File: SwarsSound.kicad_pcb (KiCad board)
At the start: 2 copper layers, 152 parts, among them P1 Main_Connector, P2 aud_con, P3 edge_con, Q1 2N3906f, Q2 2N3906f, Q3 2N3904, Q4 2N3904

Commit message: Moved a spot
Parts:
- moved P3 82.4 mm to (252.1, 123.9)

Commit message: Began board layout
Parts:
- added REF**: MountingHole2, Star_Wars_Vector_PCB:MountingHole2, F.Cu at (292.7, 39.4)
- added REF**: MountingHole2, Star_Wars_Vector_PCB:MountingHole2, F.Cu at (37.5, 47.0)
- added REF**: MountingHole, Star_Wars_Vector_PCB:MountingHole, F.Cu at (304.8, 24.1)
- added REF**: MountingHole, Star_Wars_Vector_PCB:MountingHole, F.Cu at (22.9, 24.1)
- added REF**: MountingHole, Star_Wars_Vector_PCB:MountingHole, F.Cu at (304.8, 240.0)
- added REF**: MountingHole, Star_Wars_Vector_PCB:MountingHole, F.Cu at (22.9, 240.0)
- moved P1 231.0 mm to (160.0, 225.8), turned to 180 degrees
- moved A-3 227.2 mm to (-49.0, 93.2)
- moved B-2 227.2 mm to (-38.9, 90.8)
- moved B-3 227.2 mm to (-151.5, 165.0)
- moved C-3 227.2 mm to (-81.0, 122.9)
- moved C-4 227.2 mm to (-91.1, 140.0)
- moved C/D-1 227.2 mm to (-128.0, 140.4)
- moved C1 227.2 mm to (-73.0, 150.5)
- moved C10 227.2 mm to (-67.2, 136.2)
- moved C11 227.2 mm to (-70.1, 136.2)
- moved C12 227.2 mm to (-89.0, 156.7)
- moved C16 227.2 mm to (-60.0, 127.8)
- moved C17 227.2 mm to (-39.6, 107.5)
- moved C18 227.2 mm to (-1.04, 69.4)
- moved C19 227.2 mm to (-22.2, 89.7)
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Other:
- board outline added: 292.1 x 227.3 mm

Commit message: Finished chip layout
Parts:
- removed H_2: LS04, Star_Wars_Vector_PCB:DIP14
- moved J/K-1 448.9 mm to (259.7, 73.7), turned to 180 degrees
- moved K-3 421.3 mm to (274.3, 128.3), turned to 180 degrees
- moved F/H-1 385.9 mm to (212.7, 71.1), turned to 180 degrees
- moved H-1 342.9 mm to (237.5, 73.7), turned to 180 degrees
- moved D-2 315.2 mm to (141.0, 119.4), turned to 90 degrees
- moved F-2 300.2 mm to (208.9, 114.3), turned to 180 degrees
- moved H-2 295.4 mm to (236.2, 114.3), turned to 180 degrees
- moved J-3 291.2 mm to (252.7, 138.4), turned to 180 degrees
- moved H-3 286.7 mm to (236.2, 140.3), turned to 180 degrees
- moved J-2 276.4 mm to (252.7, 113.0), turned to 180 degrees
- moved F-3 272.1 mm to (208.9, 138.4), turned to 180 degrees
- moved E-1 271.3 mm to (189.2, 87.6), turned to 180 degrees
- moved C/D-1 268.9 mm to (130.8, 67.3), turned to 180 degrees
- moved D-3 255.5 mm to (141.0, 143.5), turned to 90 degrees
- moved C32 249.2 mm to (106.7, 158.8), turned to 270 degrees
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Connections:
- A-3 pad 14: Net-(A-3-Pad14) -> +12V
- H-2 pad 10: (no net) -> ~SRES
- H-2 pad 11: (no net) -> Net-(F-5-Pad10)

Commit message: test
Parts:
- moved C27 41.9 mm to (43.2, 62.2)

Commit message: next push
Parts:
- added TP11: TP, Star_Wars_Vector_PCB:TEST_POINT, F.Cu at (207.0, 41.9)
- moved C2 310.5 mm to (259.1, 95.0), turned to 90 degrees
- moved R6 294.2 mm to (202.9, 34.0), turned to 90 degrees
- moved C5 287.5 mm to (184.9, 33.0), turned to 270 degrees
- moved R12 257.0 mm to (199.4, 110.5)
- moved C3 250.6 mm to (237.0, 95.0), turned to 90 degrees
- moved TP7 245.1 mm to (198.1, 41.9)
- moved C24 243.4 mm to (209.6, 102.9), turned to 90 degrees
- moved C4 243.1 mm to (211.6, 90.4), turned to 90 degrees
- moved R5 205.3 mm to (192.5, 44.5), turned to 180 degrees
- moved C27 39.4 mm to (3.81, 61.0)
- moved H-1 0.13 mm to (237.6, 73.7)
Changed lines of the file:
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@@
     (tracks 0)
     (zones 0)
-    (modules 157)
+    (modules 158)
     (nets 256)
   )
@@
     (add_net ɸE)
   )
+  (module Star_Wars_Vector_PCB:TEST_POINT (layer F.Cu)
+    (at 207.01 41.91)
+    (fp_text reference TP11 (at 0 0.635 90) (layer F.SilkS) hide
+      (effects (font (size 0.254 0.254) (thickness 0.0635)))
+    )
+    (fp_text value TP (at 0 -0.635 90) (layer F.Fab) hide
+      (effects (font (size 0.254 0.254) (thickness 0.0635)))
+    )
+    (pad 2 thru_hole circle (at 0 -2.54) (size 1.905 1.905) (drill 1.016) (layers *.Cu *.Mask)
+      (net 6 GND))
+    (pad 1 thru_hole circle (at 0 2.54) (size 1.905 1.905) (drill 1.016) (layers *.Cu *.Mask)
+      (net 6 GND))
+  )
   (module Star_Wars_Vector_PCB:MountingHole2 (layer F.Cu)
     (at 292.735 39.37)
@@
   )
   (module Star_Wars_Vector_PCB:TEST_POINT (layer F.Cu)
-    (at -20.3665 152.978499)
+    (at 198.12 41.91)
     (fp_text reference TP7 (at 0 0.635 90) (layer F.SilkS) hide
       (effects (font (size 0.254 0.254) (thickness 0.0635)))
@@
   )
   (module Star_Wars_Vector_PCB:GenericComp (layer F.Cu)
-    (at -55.6215 142.138499)
+    (at 199.39 110.49)
     (fp_text reference R12 (at 0 -9.525 90 unlocked) (layer F.SilkS)
       (effects (font (size 1 1) (thickness 0.15)))
@@
   )
   (module Star_Wars_Vector_PCB:GenericComp (layer F.Cu)
-    (at -67.2215 150.508499)
-    (fp_text reference R6 (at 0 -9.525 90 unlocked) (layer F.SilkS)
+    (at 202.946 34.036 90)
+    (fp_text reference R6 (at 0 -9.525 unlocked) (layer F.SilkS)
       (effects (font (size 1 1) (thickness 0.15)))
     )
-    (fp_text value 10K (at -1.27 -0.635 90) (layer F.Fab) hide
+    (fp_text value 10K (at -1.27 -0.635) (layer F.Fab) hide
       (effects (font (size 1 1) (thickness 0.15)))
     )
     (fp_line (start 0 -5.08) (end 0 3.81) (layer F.SilkS) (width 0.254))
-    (pad 2 thru_hole circle (at 0 -6.35) (size 1.905 1.905) (drill 1.016) (layers *.Cu *.Mask)
+    (pad 2 thru_hole circle (at 0 -6.35 90) (size 1.905 1.905) (drill 1.016) (layers *.Cu *.Mask)
       (net 129 "Net-(E-1-Pad12)"))
-    (pad 1 thru_hole circle (at 0 5.08) (size 1.905 1.905) (drill 1.016) (layers *.Cu *.Mask)
+    (pad 1 thru_hole circle (at 0 5.08 90) (size 1.905 1.905) (drill 1.016) (layers *.Cu *.Mask)
       (net 25 +5V))
   )
   (module Star_Wars_Vector_PCB:GenericComp (layer F.Cu)
-    (at -7.7215 89.535)
+    (at 192.532 44.45 180)
     (fp_text reference R5 (at 0 -9.525 90 unlocked) (layer F.SilkS)
       (effects (font (size 1 1) (thickness 0.15)))
@@
     )
     (fp_line (start 0 -5.08) (end 0 3.81) (layer F.SilkS) (width 0.254))
-    (pad 2 thru_hole circle (at 0 -6.35) (size 1.905 1.905) (drill 1.016) (layers *.Cu *.Mask)
+    (pad 2 thru_hole circle (at 0 -6.35 180) (size 1.905 1.905) (drill 1.016) (layers *.Cu *.Mask)
       (net 131 S~IRQ))
-    (pad 1 thru_hole circle (at 0 5.08) (size 1.905 1.905) (drill 1.016) (layers *.Cu *.Mask)
+    (pad 1 thru_hole circle (at 0 5.08 180) (size 1.905 1.905) (drill 1.016) (layers *.Cu *.Mask)
       (net 25 +5V))
   )
@@
   )
   (module Star_Wars_Main_PCB:DIP28 (layer F.Cu)
-    (at 237.49 73.66 180)
+    (at 237.617 73.66 180)
     (fp_text reference H-1 (at 0.635 -1.905 270 unlocked) (layer F.SilkS)
       (effects (font (size 1 1) (thickness 0.15)))
@@
   )
   (module Star_Wars_Vector_PCB:GenericComp (layer F.Cu)
-    (at 43.18 62.23)
+    (at 3.81 60.96)
     (fp_text reference C27 (at 0 -9.525 90 unlocked) (layer F.SilkS)
       (effects (font (size 1 1) (thickness 0.15)))
@@
   )
   (module Star_Wars_Vector_PCB:GenericComp (layer F.Cu)
-    (at -33.8015 107.508499)
-    (fp_text reference C24 (at 0 -9.525 90 unlocked) (layer F.SilkS)
+    (at 209.55 102.87 90)
+    (fp_text reference C24 (at 0 8.89 unlocked) (layer F.SilkS)
       (effects (font (size 1 1) (thickness 0.15)))
     )
-    (fp_text value 0.1 (at -1.27 -0.635 90) (layer F.Fab) hide
+    (fp_text value 0.1 (at -1.27 -0.635) (layer F.Fab) hide
       (effects (font (size 1 1) (thickness 0.15)))
     )
     (fp_line (start 0 -5.08) (end 0 3.81) (layer F.SilkS) (width 0.254))
-    (pad 2 thru_hole circle (at 0 -6.35) (size 1.905 1.905) (drill 1.016) (layers *.Cu *.Mask)
+    (pad 2 thru_hole circle (at 0 -6.35 90) (size 1.905 1.905) (drill 1.016) (layers *.Cu *.Mask)
       (net 6 GND))
-    (pad 1 thru_hole circle (at 0 5.08) (size 1.905 1.905) (drill 1.016) (layers *.Cu *.Mask)
+    (pad 1 thru_hole circle (at 0 5.08 90) (size 1.905 1.905) (drill 1.016) (layers *.Cu *.Mask)
       (net 12 -5V))
   )
@@
   )
   (module Star_Wars_Vector_PCB:GenericComp (layer F.Cu)
-    (at -75.9215 153.938499)
-    (fp_text reference C5 (at 0 -9.525 90 unlocked) (layer F.SilkS)
+    (at 184.912 33.02 270)
+    (fp_text reference C5 (at -0.508 8.636 unlocked) (layer F.SilkS)
       (effects (font (size 1 1) (thickness 0.15)))
     )
-    (fp_text value 0.1uf (at -1.27 -0.635 90) (layer F.Fab) hide
+    (fp_text value 0.1uf (at -1.27 -0.635) (layer F.Fab) hide
       (effects (font (size 1 1) (thickness 0.15)))
     )
     (fp_line (start 0 -5.08) (end 0 3.81) (layer F.SilkS) (width 0.254))
-    (pad 2 thru_hole circle (at 0 -6.35) (size 1.905 1.905) (drill 1.016) (layers *.Cu *.Mask)
+    (pad 2 thru_hole circle (at 0 -6.35 270) (size 1.905 1.905) (drill 1.016) (layers *.Cu *.Mask)
       (net 25 +5V))
-    (pad 1 thru_hole circle (at 0 5.08) (size 1.905 1.905) (drill 1.016) (layers *.Cu *.Mask)
+    (pad 1 thru_hole circle (at 0 5.08 270) (size 1.905 1.905) (drill 1.016) (layers *.Cu *.Mask)
       (net 6 GND))
   )
   (module Star_Wars_Vector_PCB:GenericComp (layer F.Cu)
-    (at -30.9015 107.508499)
-    (fp_text reference C4 (at 0 -9.525 90 unlocked) (layer F.SilkS)
+    (at 211.582 90.424 90)
+    (fp_text reference C4 (at 0 -9.525 unlocked) (layer F.SilkS)
       (effects (font (size 1 1) (thickness 0.15)))
     )
-    (fp_text value 0.1uf (at -1.27 -0.635 90) (layer F.Fab) hide
+    (fp_text value 0.1uf (at -1.27 -0.635) (layer F.Fab) hide
       (effects (font (size 1 1) (thickness 0.15)))
     )
     (fp_line (start 0 -5.08) (end 0 3.81) (layer F.SilkS) (width 0.254))
-    (pad 2 thru_hole circle (at 0 -6.35) (size 1.905 1.905) (drill 1.016) (layers *.Cu *.Mask)
+    (pad 2 thru_hole circle (at 0 -6.35 90) (size 1.905 1.905) (drill 1.016) (layers *.Cu *.Mask)
       (net 25 +5V))
-    (pad 1 thru_hole circle (at 0 5.08) (size 1.905 1.905) (drill 1.016) (layers *.Cu *.Mask)
+    (pad 1 thru_hole circle (at 0 5.08 90) (size 1.905 1.905) (drill 1.016) (layers *.Cu *.Mask)
       (net 6 GND))
   )
   (module Star_Wars_Vector_PCB:GenericComp (layer F.Cu)
-    (at -13.5215 89.748499)
-    (fp_text reference C3 (at 0 -9.525 90 unlocked) (layer F.SilkS)
+    (at 236.982 94.996 90)
+    (fp_text reference C3 (at 0 -9.525 unlocked) (layer F.SilkS)
       (effects (font (size 1 1) (thickness 0.15)))
     )
-    (fp_text value 0.1uf (at -1.27 -0.635 90) (layer F.Fab) hide
+    (fp_text value 0.1uf (at -1.27 -0.635) (layer F.Fab) hide
       (effects (font (size 1 1) (thickness 0.15)))
     )
     (fp_line (start 0 -5.08) (end 0 3.81) (layer F.SilkS) (width 0.254))
-    (pad 2 thru_hole circle (at 0 -6.35) (size 1.905 1.905) (drill 1.016) (layers *.Cu *.Mask)
+    (pad 2 thru_hole circle (at 0 -6.35 90) (size 1.905 1.905) (drill 1.016) (layers *.Cu *.Mask)
       (net 25 +5V))
-    (pad 1 thru_hole circle (at 0 5.08) (size 1.905 1.905) (drill 1.016) (layers *.Cu *.Mask)
+    (pad 1 thru_hole circle (at 0 5.08 90) (size 1.905 1.905) (drill 1.016) (layers *.Cu *.Mask)
       (net 6 GND))
   )
   (module Star_Wars_Vector_PCB:GenericComp (layer F.Cu)
-    (at -49.7415 127.658499)
-    (fp_text reference C2 (at 0 -9.525 90 unlocked) (layer F.SilkS)
+    (at 259.08 94.996 90)
+    (fp_text reference C2 (at 0 -9.525 unlocked) (layer F.SilkS)
       (effects (font (size 1 1) (thickness 0.15)))
     )
-    (fp_text value 0.1uf (at -1.27 -0.635 90) (layer F.Fab) hide
+    (fp_text value 0.1uf (at -1.27 -0.635) (layer F.Fab) hide
       (effects (font (size 1 1) (thickness 0.15)))
     )
     (fp_line (start 0 -5.08) (end 0 3.81) (layer F.SilkS) (width 0.254))
-    (pad 2 thru_hole circle (at 0 -6.35) (size 1.905 1.905) (drill 1.016) (layers *.Cu *.Mask)
+    (pad 2 thru_hole circle (at 0 -6.35 90) (size 1.905 1.905) (drill 1.016) (layers *.Cu *.Mask)
       (net 25 +5V))
-    (pad 1 thru_hole circle (at 0 5.08) (size 1.905 1.905) (drill 1.016) (layers *.Cu *.Mask)
+    (pad 1 thru_hole circle (at 0 5.08 90) (size 1.905 1.905) (drill 1.016) (layers *.Cu *.Mask)
       (net 6 GND))
   )

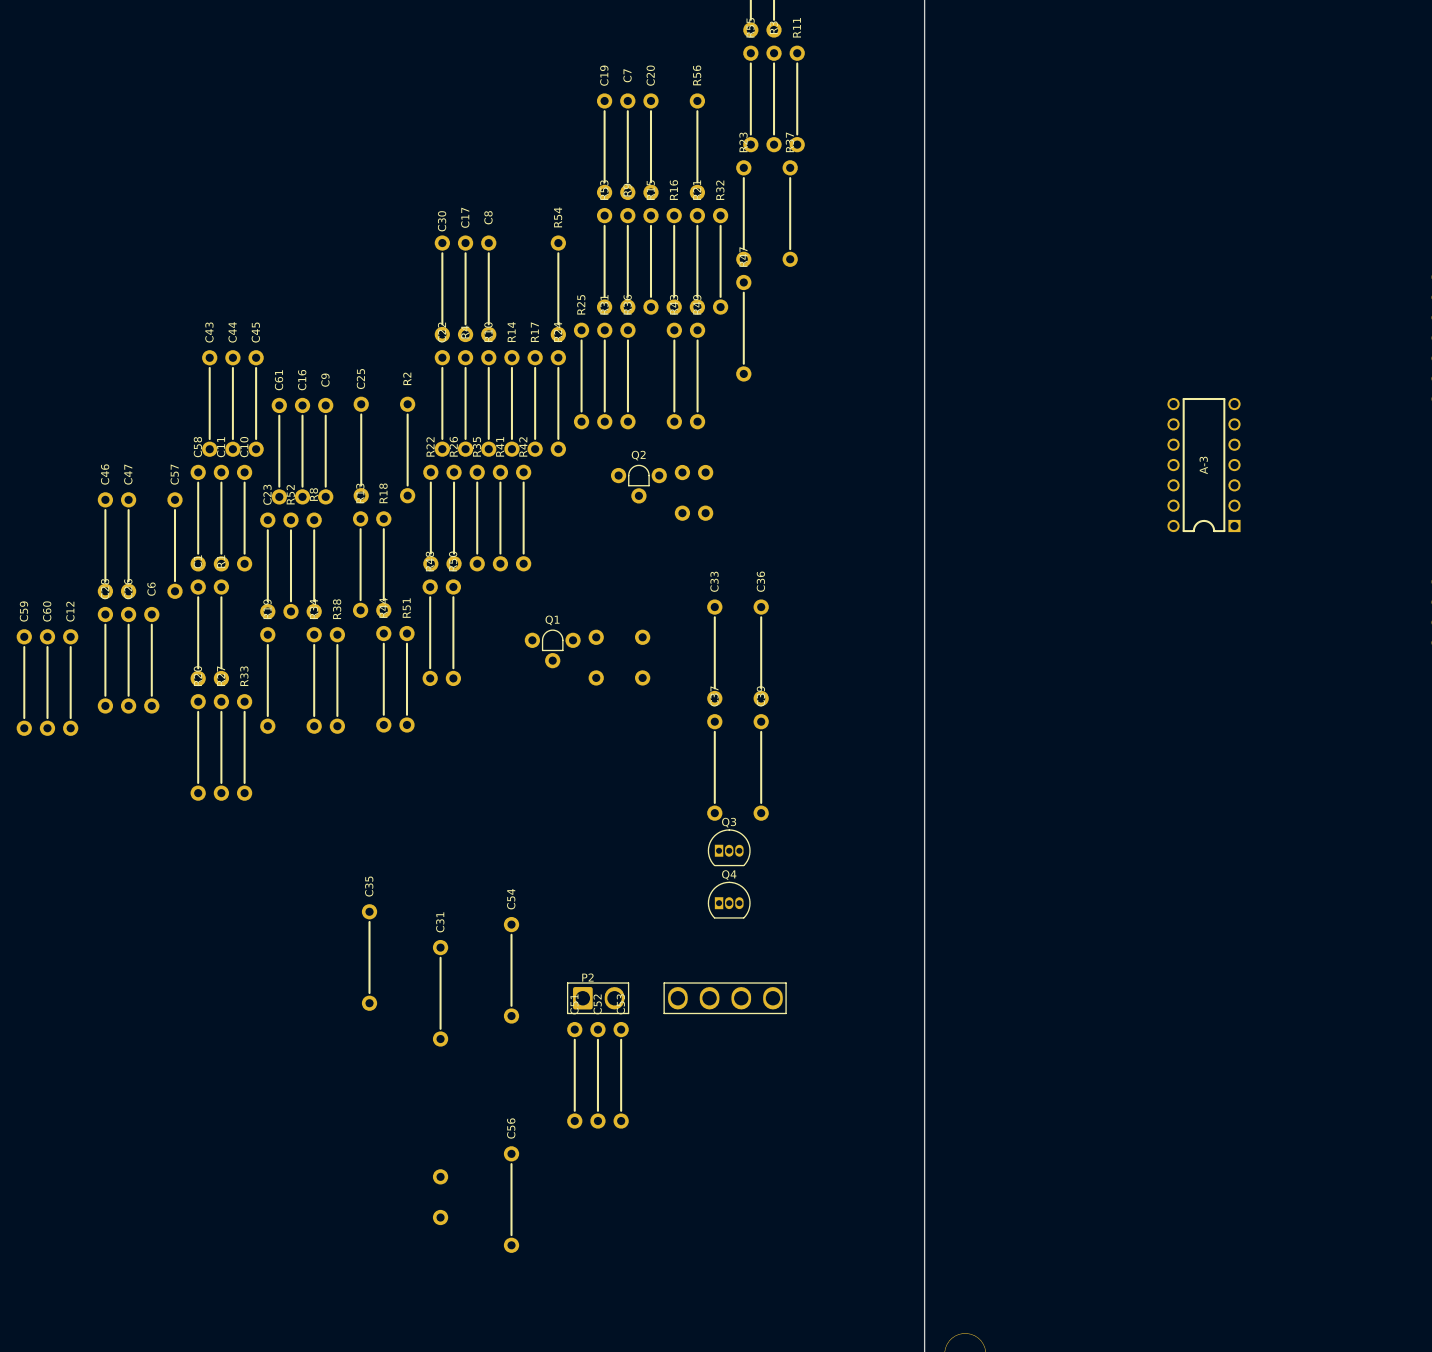
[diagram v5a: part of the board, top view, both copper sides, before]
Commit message: Added TPs and large caps
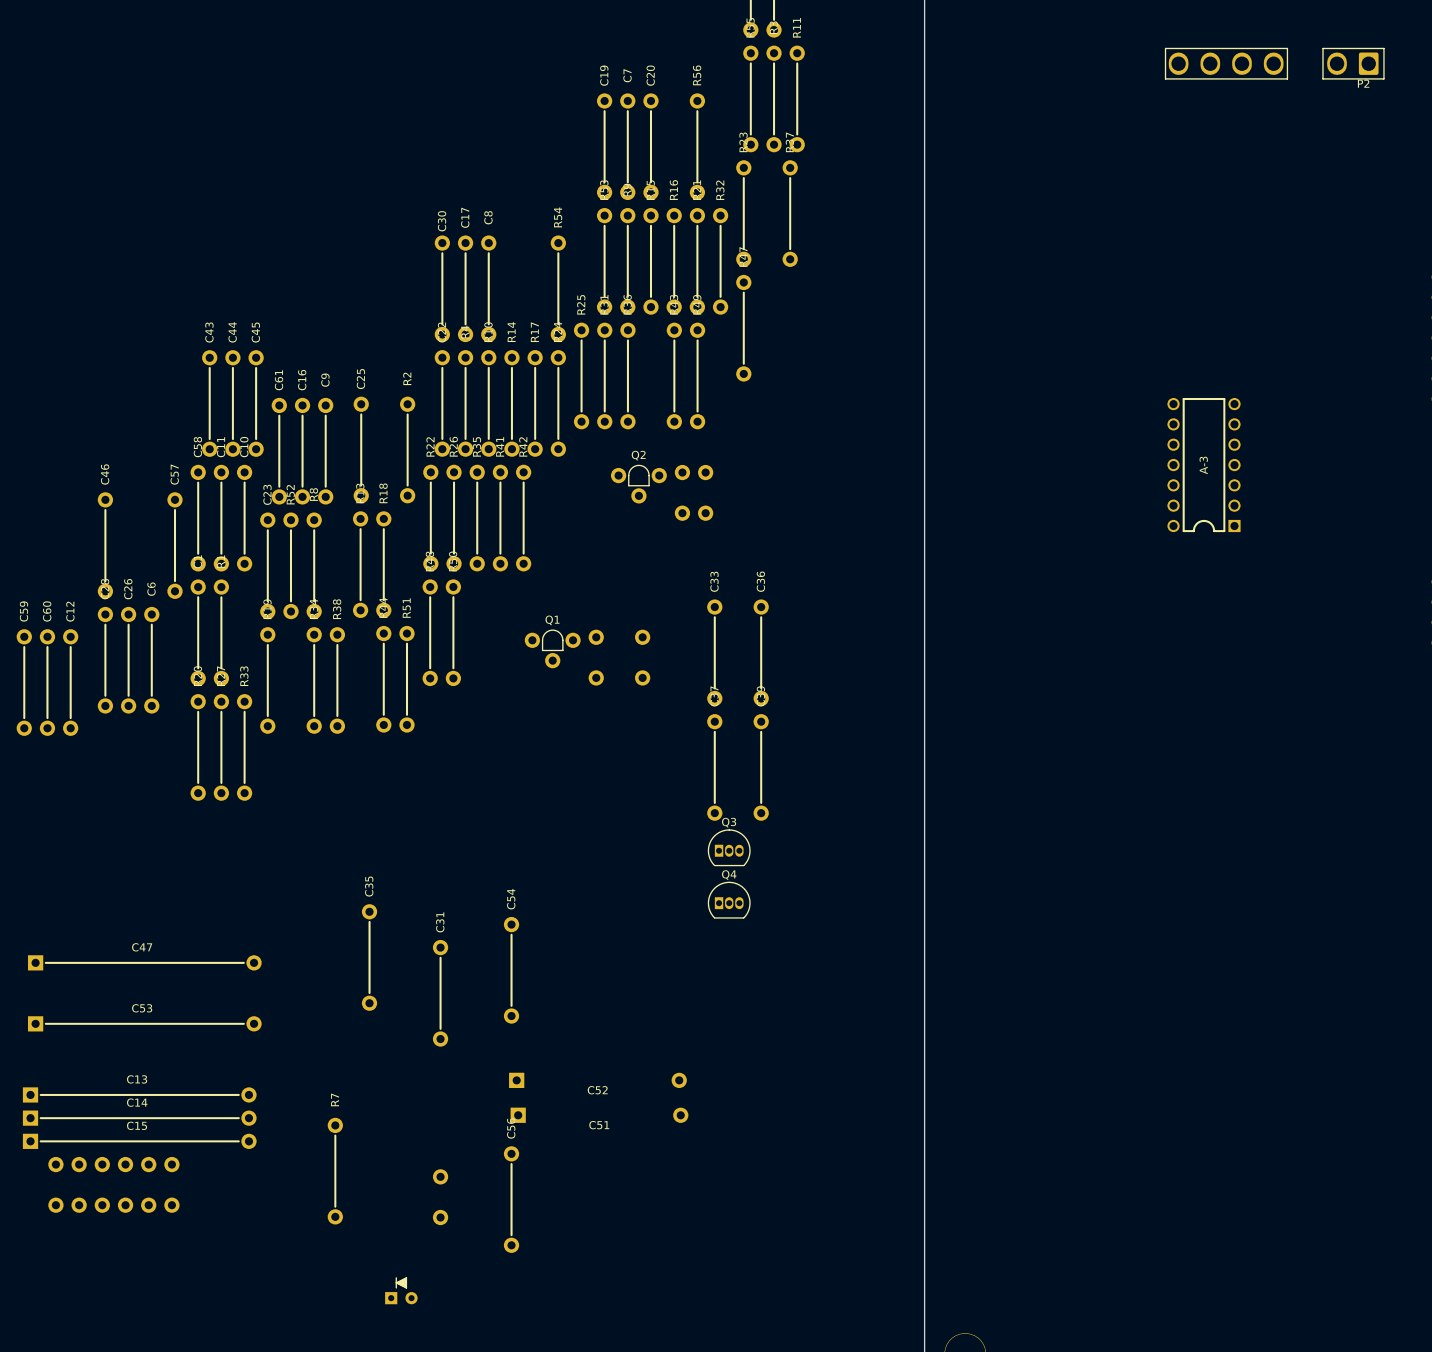
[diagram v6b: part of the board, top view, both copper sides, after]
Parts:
- added C13: 100, Star_Wars_Vector_PCB:LargeCap, F.Cu at (-80.6, 207.6)
- added C14: 100, Star_Wars_Vector_PCB:LargeCap, F.Cu at (-80.6, 210.5)
- added C15: 100, Star_Wars_Vector_PCB:LargeCap, F.Cu at (-80.6, 213.4)
- added DS1: LED, Star_Wars_Vector_PCB:LED, F.Cu at (-47.6, 233.0)
- added R7: 150, Star_Wars_Vector_PCB:GenericComp, F.Cu at (-55.9, 217.8)
- added TP11: TP, Star_Wars_Vector_PCB:TEST_POINT, F.Cu at (-79.2, 218.9)
- added TP12: TP, Star_Wars_Vector_PCB:TEST_POINT, F.Cu at (-76.3, 218.9)
- added TP3: TP, Star_Wars_Vector_PCB:TEST_POINT, F.Cu at (-90.8, 218.9)
- added TP4: TP, Star_Wars_Vector_PCB:TEST_POINT, F.Cu at (-87.9, 218.9)
- added TP5: TP, Star_Wars_Vector_PCB:TEST_POINT, F.Cu at (-85.0, 218.9)
- added TP6: TP, Star_Wars_Vector_PCB:TEST_POINT, F.Cu at (-82.1, 218.9)
- C47, C53: footprint Star_Wars_Vector_PCB:GenericComp -> Star_Wars_Vector_PCB:LargeCap
- C51, C52: footprint Star_Wars_Vector_PCB:GenericComp -> Star_Wars_Main_PCB:Cap1
- moved P2 135.5 mm to (57.4, 78.1), turned to 180 degrees
- moved C53 60.3 mm to (-80.0, 198.8)
- moved C47 51.6 mm to (-80.0, 191.1)
- moved C51 5.35 mm to (-22.9, 210.2)

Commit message: right to left to C14 Placed
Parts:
- moved C12 381.4 mm to (290.8, 191.8), turned to 90 degrees
- moved C1 365.5 mm to (292.1, 134.6), turned to 90 degrees
- moved R2 339.5 mm to (292.1, 147.3), turned to 90 degrees
- moved C11 308.0 mm to (237.5, 151.1), turned to 90 degrees
- moved C10 304.9 mm to (237.5, 125.7), turned to 90 degrees
- moved C8 302.7 mm to (254.0, 191.8), turned to 90 degrees
- moved C9 300.9 mm to (237.5, 189.2), turned to 90 degrees
- moved R1 300.9 mm to (228.6, 186.7)
- moved R3 300.5 mm to (292.1, 149.9), turned to 90 degrees
- moved C61 289.2 mm to (219.7, 189.2), turned to 270 degrees
- moved C6 288.3 mm to (207.0, 191.8), turned to 90 degrees
- moved C20 277.3 mm to (254.0, 151.1), turned to 90 degrees
- moved C7 274.4 mm to (252.7, 125.7), turned to 270 degrees
- moved C23 273.1 mm to (208.3, 125.7), turned to 270 degrees
- moved C16 258.3 mm to (189.2, 195.6), turned to 90 degrees
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
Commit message: All components placed
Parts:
- moved TP12 375.8 mm to (294.6, 158.8), turned to 270 degrees
- moved TP1 347.2 mm to (294.6, 138.4), turned to 270 degrees
- moved TP2 318.0 mm to (294.6, 143.5), turned to 270 degrees
- moved C15 183.6 mm to (30.5, 67.3), turned to 90 degrees
- moved C59 179.0 mm to (81.3, 124.5), turned to 270 degrees
- moved TP4 177.1 mm to (47.0, 104.1), turned to 270 degrees
- moved TP5 176.4 mm to (44.5, 99.1), turned to 270 degrees
- moved TP6 176.0 mm to (41.9, 94.0), turned to 270 degrees
- moved C60 175.7 mm to (81.3, 127.0), turned to 270 degrees
- moved TP3 172.3 mm to (29.2, 95.2), turned to 270 degrees
- moved C57 171.6 mm to (94.0, 115.6), turned to 270 degrees
- moved C58 169.0 mm to (94.0, 110.5), turned to 270 degrees
- moved C56 164.3 mm to (94.0, 118.1), turned to 270 degrees
- moved R51 147.1 mm to (86.4, 94.0)
- moved R48 146.4 mm to (95.2, 105.4), turned to 90 degrees
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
